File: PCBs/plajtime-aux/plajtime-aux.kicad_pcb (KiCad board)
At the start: 2 copper layers, 50.7 x 23.5 mm, 21 parts, among them J1 Slider, J2 USB, J3 Internal connector, J4 LRA, U1 USBLC6-2P6, U2 IQS7222B, U3 DA7280

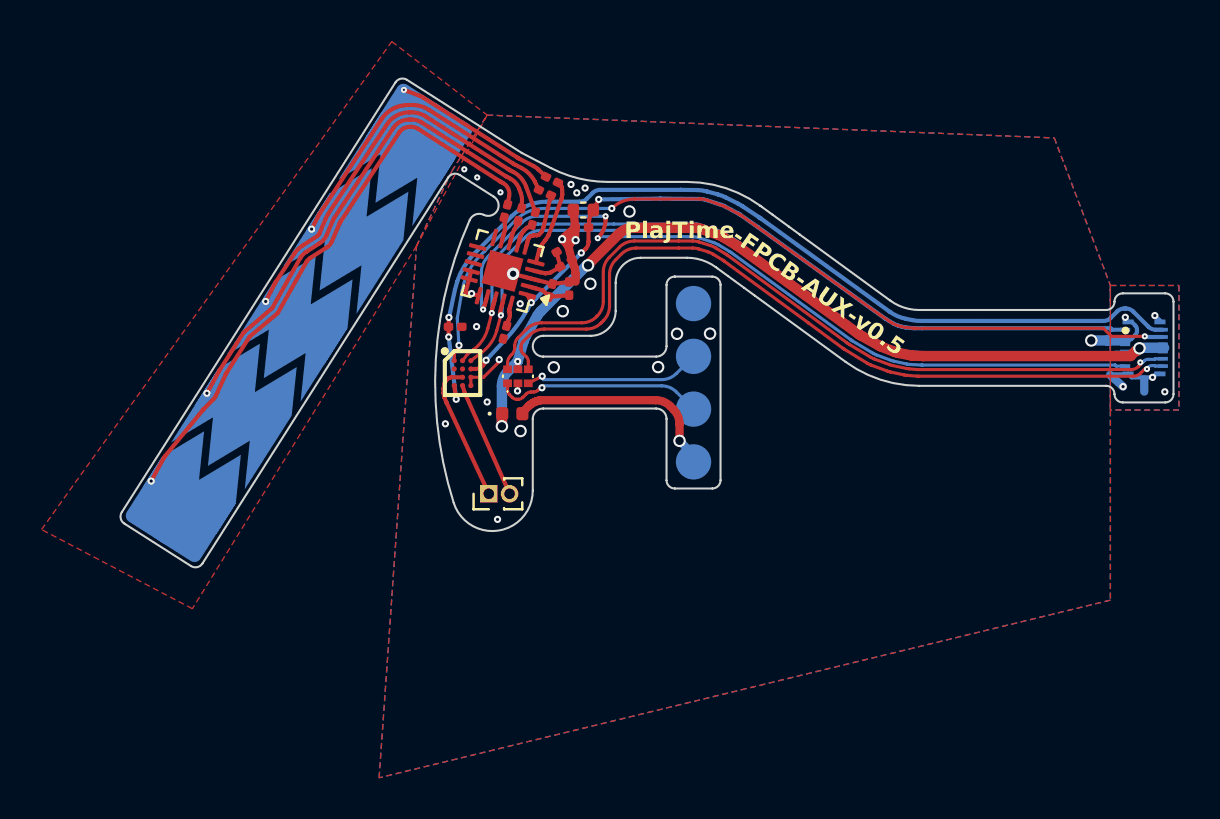
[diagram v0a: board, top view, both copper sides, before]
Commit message: Add graphics for AUX FPCB
Redo asset README a bit and move assets

Remove the pogo pins from the solderpaste layer
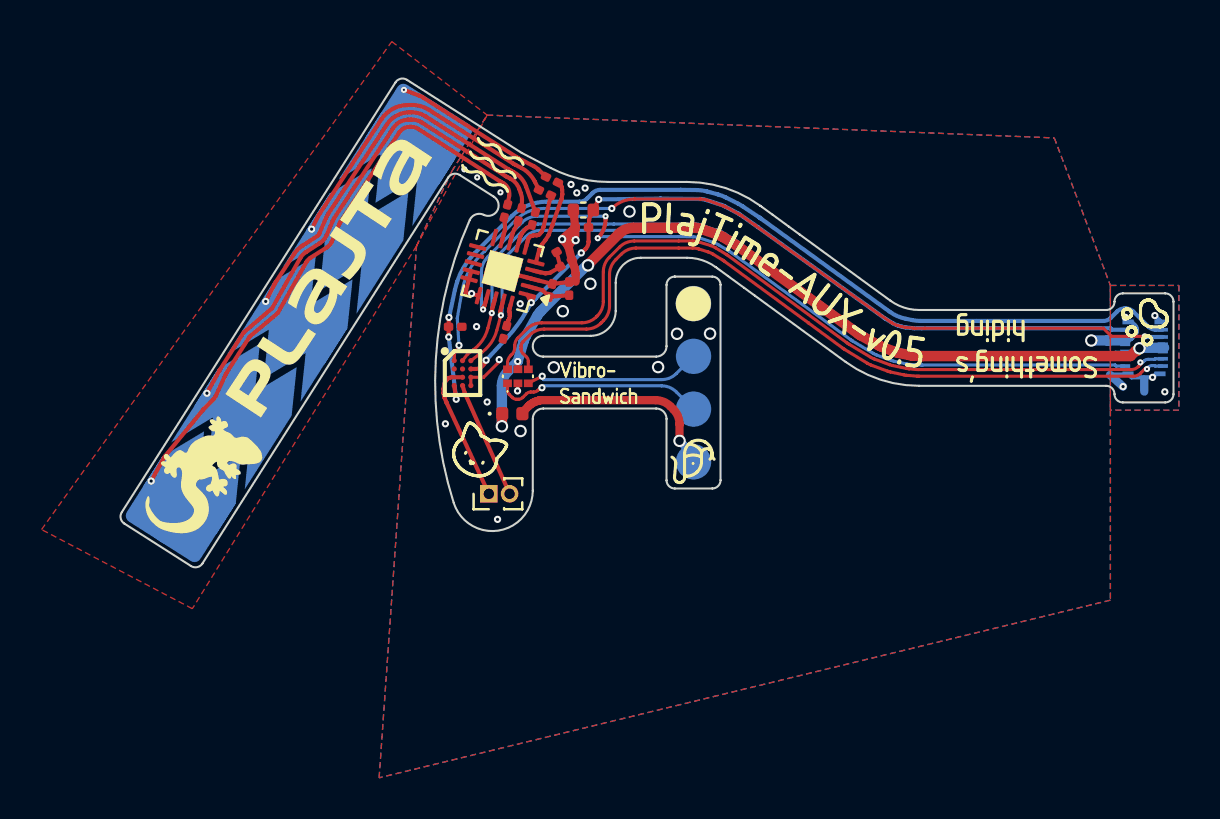
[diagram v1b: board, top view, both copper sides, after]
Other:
- board text removed: "-FPCB-AUX-v0.5"
- board text removed: "PlajTime"
